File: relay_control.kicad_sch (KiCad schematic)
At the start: 12 parts, among them U3 TLP3546, U4 TLP3546, U5 TLP3546, U6 TLP3546

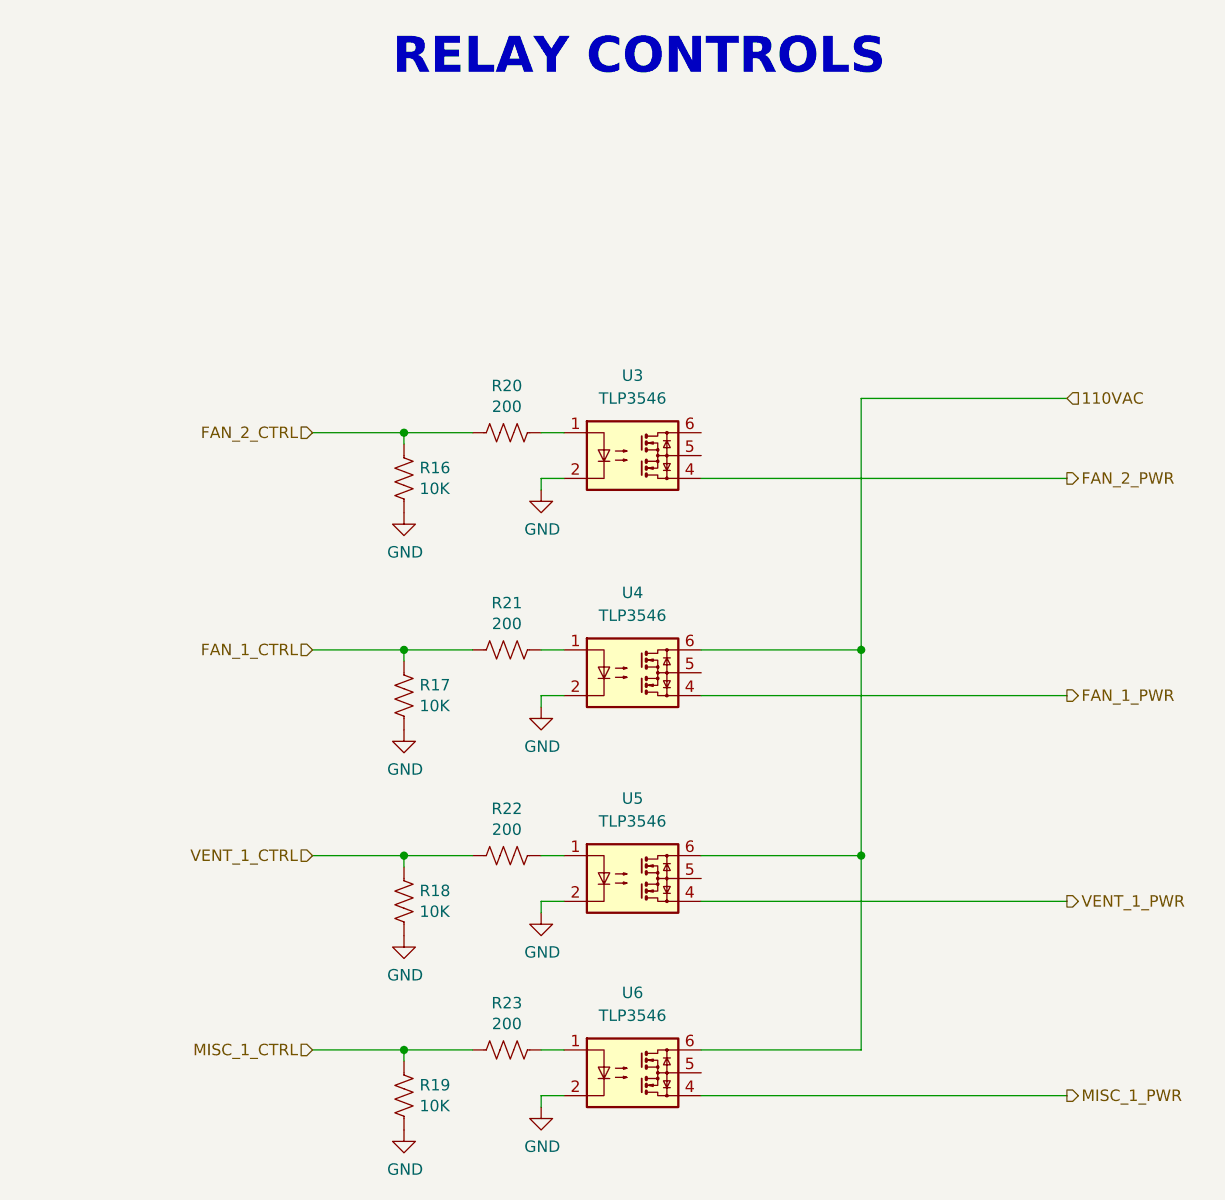
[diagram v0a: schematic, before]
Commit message: Added clamping diode for 24V net.
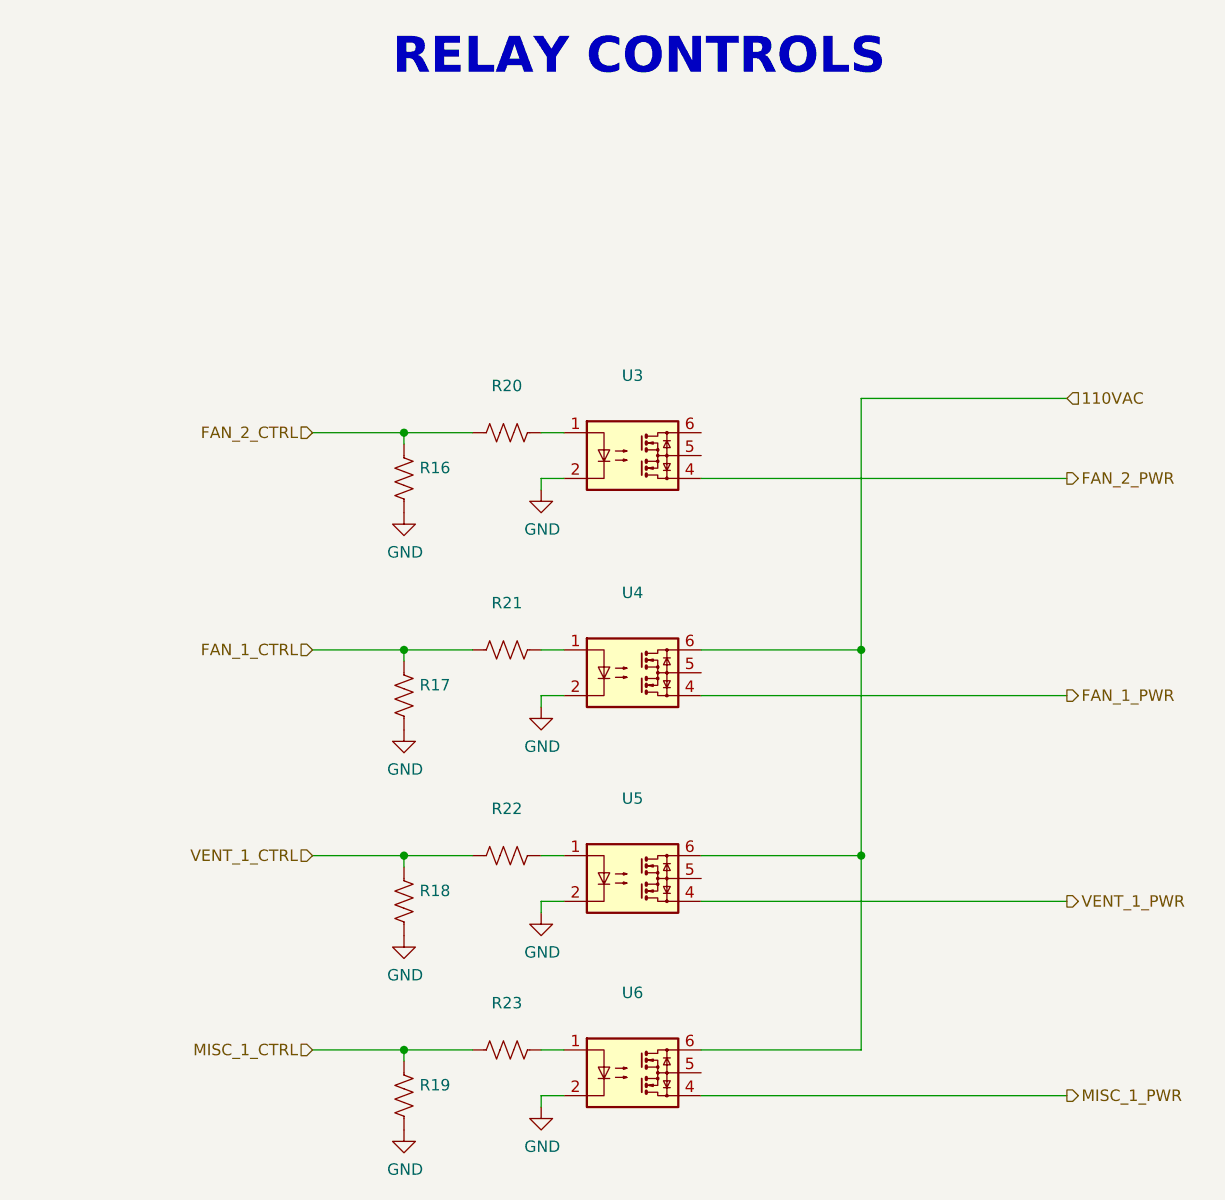
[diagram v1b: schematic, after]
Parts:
- R16, R17, R18, R19: value 10K -> (none); footprint Resistor_SMD:R_0805_2012Metric -> (none)
- R20, R21, R22, R23: value 200 -> (none); footprint Resistor_SMD:R_0805_2012Metric -> (none)
- U3, U4, U5, U6: value TLP3546 -> (none); footprint Package_DIP:DIP-6_W7.62mm -> (none)
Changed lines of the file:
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@@
     (in_bom yes) (on_board yes)
     (property "Reference" "R21" (id 0) (at 137.16 87.503 90))
-    (property "Value" "200" (id 1) (at 137.16 89.8144 90))
-    (property "Footprint" "Resistor_SMD:R_0805_2012Metric" (id 2) (at 136.906 93.726 90)
+    (property "Value" "" (id 1) (at 137.16 89.8144 90))
+    (property "Footprint" "" (id 2) (at 136.906 93.726 90)
       (effects (font (size 1.27 1.27)) hide)
     )
@@
       (effects (font (size 1.27 1.27)) (justify left))
     )
-    (property "Value" "10K" (id 1) (at 127.4572 98.933 0)
-      (effects (font (size 1.27 1.27)) (justify left))
-    )
-    (property "Footprint" "Resistor_SMD:R_0805_2012Metric" (id 2) (at 126.746 98.044 90)
+    (property "Value" "" (id 1) (at 127.4572 98.933 0)
+      (effects (font (size 1.27 1.27)) (justify left))
+    )
+    (property "Footprint" "" (id 2) (at 126.746 98.044 90)
       (effects (font (size 1.27 1.27)) hide)
     )
@@
     (in_bom yes) (on_board yes)
     (property "Reference" "R20" (id 0) (at 137.16 63.373 90))
-    (property "Value" "200" (id 1) (at 137.16 65.6844 90))
-    (property "Footprint" "Resistor_SMD:R_0805_2012Metric" (id 2) (at 136.906 69.596 90)
+    (property "Value" "" (id 1) (at 137.16 65.6844 90))
+    (property "Footprint" "" (id 2) (at 136.906 69.596 90)
       (effects (font (size 1.27 1.27)) hide)
     )
@@
       (effects (font (size 1.27 1.27)) (justify left))
     )
-    (property "Value" "10K" (id 1) (at 127.4572 74.803 0)
-      (effects (font (size 1.27 1.27)) (justify left))
-    )
-    (property "Footprint" "Resistor_SMD:R_0805_2012Metric" (id 2) (at 126.746 73.914 90)
+    (property "Value" "" (id 1) (at 127.4572 74.803 0)
+      (effects (font (size 1.27 1.27)) (justify left))
+    )
+    (property "Footprint" "" (id 2) (at 126.746 73.914 90)
       (effects (font (size 1.27 1.27)) hide)
     )
@@
     (in_bom yes) (on_board yes)
     (property "Reference" "R22" (id 0) (at 137.16 110.363 90))
-    (property "Value" "200" (id 1) (at 137.16 112.6744 90))
-    (property "Footprint" "Resistor_SMD:R_0805_2012Metric" (id 2) (at 136.906 116.586 90)
+    (property "Value" "" (id 1) (at 137.16 112.6744 90))
+    (property "Footprint" "" (id 2) (at 136.906 116.586 90)
       (effects (font (size 1.27 1.27)) hide)
     )
@@
       (effects (font (size 1.27 1.27)) (justify left))
     )
-    (property "Value" "10K" (id 1) (at 127.4572 121.793 0)
-      (effects (font (size 1.27 1.27)) (justify left))
-    )
-    (property "Footprint" "Resistor_SMD:R_0805_2012Metric" (id 2) (at 126.746 120.904 90)
+    (property "Value" "" (id 1) (at 127.4572 121.793 0)
+      (effects (font (size 1.27 1.27)) (justify left))
+    )
+    (property "Footprint" "" (id 2) (at 126.746 120.904 90)
       (effects (font (size 1.27 1.27)) hide)
     )
@@
     (in_bom yes) (on_board yes)
     (property "Reference" "R23" (id 0) (at 137.16 131.953 90))
-    (property "Value" "200" (id 1) (at 137.16 134.2644 90))
-    (property "Footprint" "Resistor_SMD:R_0805_2012Metric" (id 2) (at 136.906 138.176 90)
+    (property "Value" "" (id 1) (at 137.16 134.2644 90))
+    (property "Footprint" "" (id 2) (at 136.906 138.176 90)
       (effects (font (size 1.27 1.27)) hide)
     )
@@
       (effects (font (size 1.27 1.27)) (justify left))
     )
-    (property "Value" "10K" (id 1) (at 127.4572 143.383 0)
-      (effects (font (size 1.27 1.27)) (justify left))
-    )
-    (property "Footprint" "Resistor_SMD:R_0805_2012Metric" (id 2) (at 126.746 142.494 90)
+    (property "Value" "" (id 1) (at 127.4572 143.383 0)
+      (effects (font (size 1.27 1.27)) (justify left))
+    )
+    (property "Footprint" "" (id 2) (at 126.746 142.494 90)
       (effects (font (size 1.27 1.27)) hide)
     )
@@
     (in_bom yes) (on_board yes) (fields_autoplaced)
     (property "Reference" "U5" (id 0) (at 151.13 109.22 0))
-    (property "Value" "TLP3546" (id 1) (at 151.13 111.76 0))
-    (property "Footprint" "Package_DIP:DIP-6_W7.62mm" (id 2) (at 151.13 125.73 0)
+    (property "Value" "" (id 1) (at 151.13 111.76 0))
+    (property "Footprint" "" (id 2) (at 151.13 125.73 0)
       (effects (font (size 1.27 1.27)) hide)
     )
@@
     (in_bom yes) (on_board yes) (fields_autoplaced)
     (property "Reference" "U4" (id 0) (at 151.13 86.36 0))
-    (property "Value" "TLP3546" (id 1) (at 151.13 88.9 0))
-    (property "Footprint" "Package_DIP:DIP-6_W7.62mm" (id 2) (at 151.13 102.87 0)
+    (property "Value" "" (id 1) (at 151.13 88.9 0))
+    (property "Footprint" "" (id 2) (at 151.13 102.87 0)
       (effects (font (size 1.27 1.27)) hide)
     )
@@
     (in_bom yes) (on_board yes) (fields_autoplaced)
     (property "Reference" "U3" (id 0) (at 151.13 62.23 0))
-    (property "Value" "TLP3546" (id 1) (at 151.13 64.77 0))
-    (property "Footprint" "Package_DIP:DIP-6_W7.62mm" (id 2) (at 151.13 78.74 0)
+    (property "Value" "" (id 1) (at 151.13 64.77 0))
+    (property "Footprint" "" (id 2) (at 151.13 78.74 0)
       (effects (font (size 1.27 1.27)) hide)
     )
@@
     (in_bom yes) (on_board yes) (fields_autoplaced)
     (property "Reference" "U6" (id 0) (at 151.13 130.81 0))
-    (property "Value" "TLP3546" (id 1) (at 151.13 133.35 0))
-    (property "Footprint" "Package_DIP:DIP-6_W7.62mm" (id 2) (at 151.13 147.32 0)
-      (effects (font (size 1.27 1.27)) hide)
-    )
+    (property "Value" "" (id 1) (at 151.13 133.35 0))
+    (property "Footprint" "" (id 2) (at 151.13 147.32 0)
+      (effects (font (size 1.27 1.27)) hide)
+    )

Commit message: Continued with layout.
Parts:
- removed U3, U4, U5, U6: (no value), symbol Relay_SolidState:TLP3546
- added U3, U4, U5, U6: (no value), symbol TLP3825:TLP3825TP1_F
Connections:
- net 110VAC: now also U3.8 (DRAIN), U4.8 (DRAIN), U5.8 (DRAIN), U6.8 (DRAIN)
- net FAN_1_PWR: now also U4.5 (DRAIN)
- net FAN_2_PWR: now also U3.5 (DRAIN)
- net GND: now also U3.3 (CATHODE), U4.3 (CATHODE), U5.3 (CATHODE), U6.3 (CATHODE)
- net MISC_1_PWR: now also U6.5 (DRAIN)
- net VENT_1_PWR: now also U5.5 (DRAIN)
- net at R21.1: now also U4.2 (ANODE)
- net at R20.1: now also U3.2 (ANODE)
- net at R22.1: now also U5.2 (ANODE)
- net at R23.1: now also U6.2 (ANODE)
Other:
- moved on the sheet: R16, R17, R18, R19, R20, R21, R22, R23
